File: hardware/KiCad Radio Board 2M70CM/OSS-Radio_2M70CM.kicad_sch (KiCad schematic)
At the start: 110 parts, among them J1 DF40C-24DP-0.4V, Q1 BSS138, Q2 BSS138, Q3 BSS138, U3 GRF5504, U4 TPS7A4701xRGW, U5 CC1200, U6 AT24CS01-STUM, U7 SKY13330-397LF, Y4 TG-5021CG

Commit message: changed mounting holes on 2M70CM board
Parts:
- removed TP4: TestPoint, TestPoint:TestPoint_Pad_D1.0mm, symbol Connector:TestPoint
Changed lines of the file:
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@@
 	)
 	(junction
-		(at 243.84 26.67)
-		(diameter 0)
-		(color 0 0 0 0)
-	)
-	(junction
 		(at 121.92 158.75)
 		(diameter 0)
@@
 	(wire
 		(pts
-			(xy 228.6 26.67) (xy 243.84 26.67)
+			(xy 228.6 26.67) (xy 246.38 26.67)
 		)
 		(stroke
@@
 	(wire
 		(pts
-			(xy 243.84 26.67) (xy 246.38 26.67)
-		)
-		(stroke
-			(width 0)
-			(type default)
-		)
-	)
-	(wire
-		(pts
 			(xy 147.32 93.98) (xy 180.34 93.98)
 		)
@@
 					(unit 1)
 				)
-			)
-		)
-	)
-	(symbol
-		(lib_id "Connector:TestPoint")
-		(at 243.84 26.67 180)
-		(unit 1)
-		(exclude_from_sim no)
-		(in_bom no)
-		(on_board yes)
-		(dnp no)
-		(fields_autoplaced yes)
-		(property "Reference" "TP4"
-			(at 246.38 28.7019 0)
-			(effects
-				(font
-					(size 1.27 1.27)
-				)
-				(justify right)
-			)
-		)
-		(property "Value" "TestPoint"
-			(at 246.38 31.2419 0)
-			(effects
-				(font
-					(size 1.27 1.27)
-				)
-				(justify right)
-			)
-		)
-		(property "Footprint" "TestPoint:TestPoint_Pad_D1.0mm"
-			(at 238.76 26.67 0)
-			(effects
-				(font
-					(size 1.27 1.27)
-				)
-				(hide yes)
-			)
-		)
-		(property "Datasheet" "~"
-			(at 238.76 26.67 0)
-			(effects
-				(font
-					(size 1.27 1.27)
-				)
-				(hide yes)
-			)
-		)
-		(property "Description" "test point"
-			(at 243.84 26.67 0)
-			(effects
-				(font
-					(size 1.27 1.27)
-				)
-				(hide yes)
-			)
-		)
-		(pin "1"
-		)
-		(instances
-			(project "OSS-Radio_2M70CM"
-				(path "/07417920-d864-4fe6-bbe4-9feb9e01fbee"
-					(reference "TP4")
-					(unit 1)
-				)

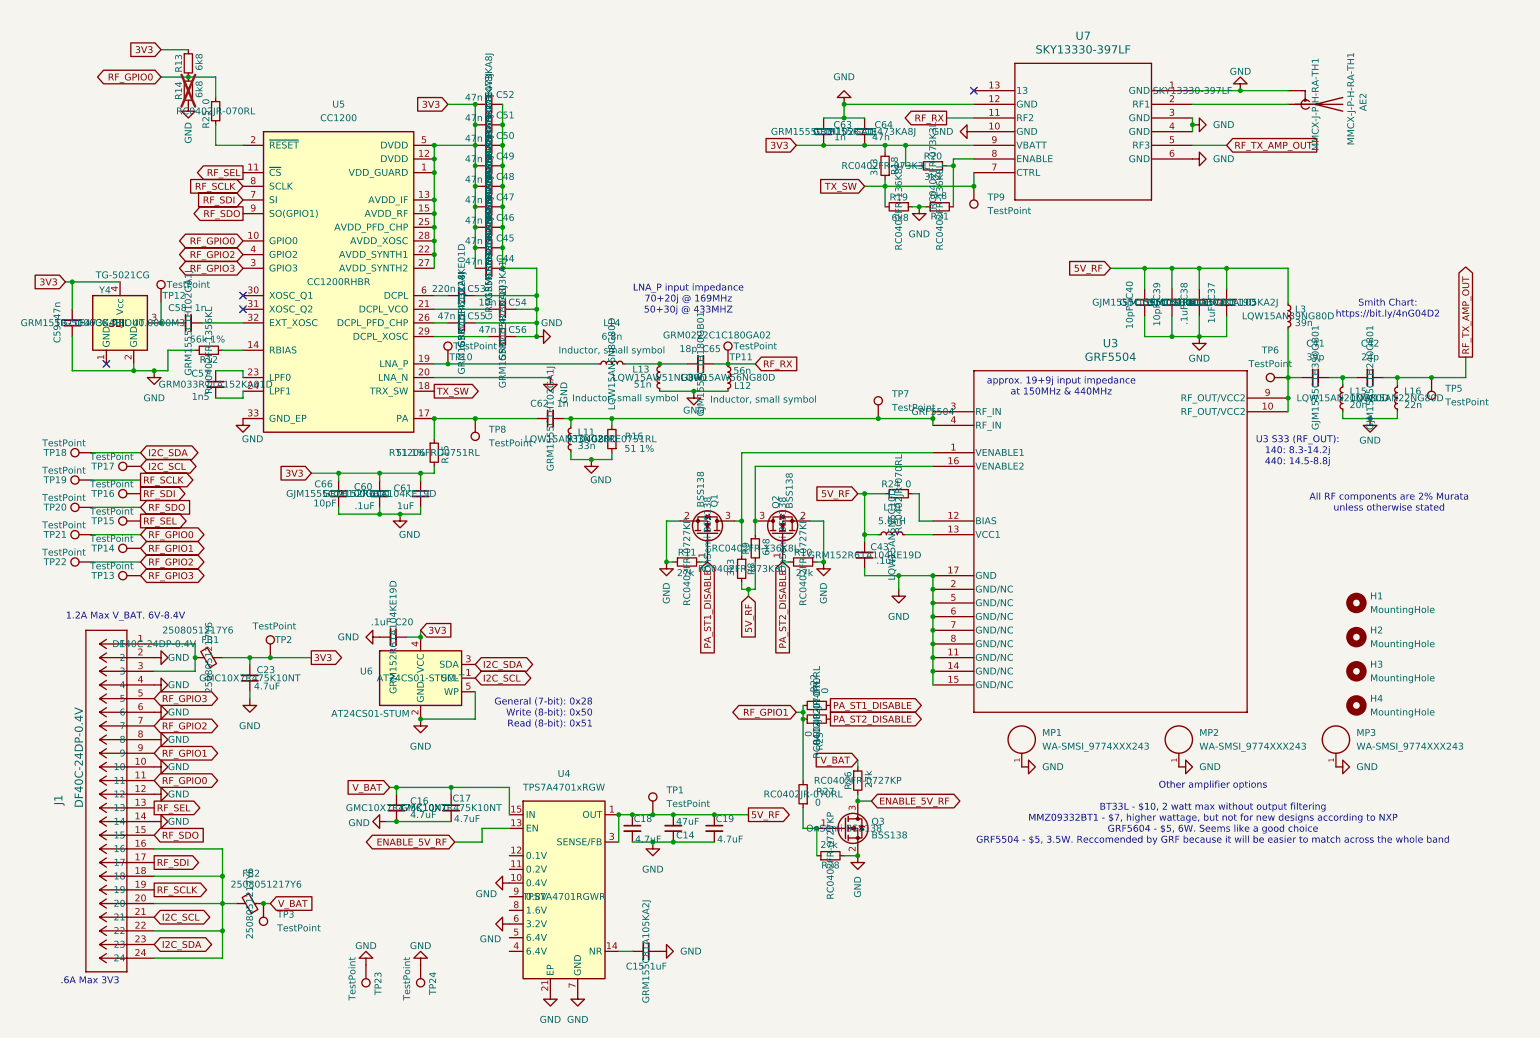
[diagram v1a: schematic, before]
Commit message: changed schematic annotations to not show part numbers
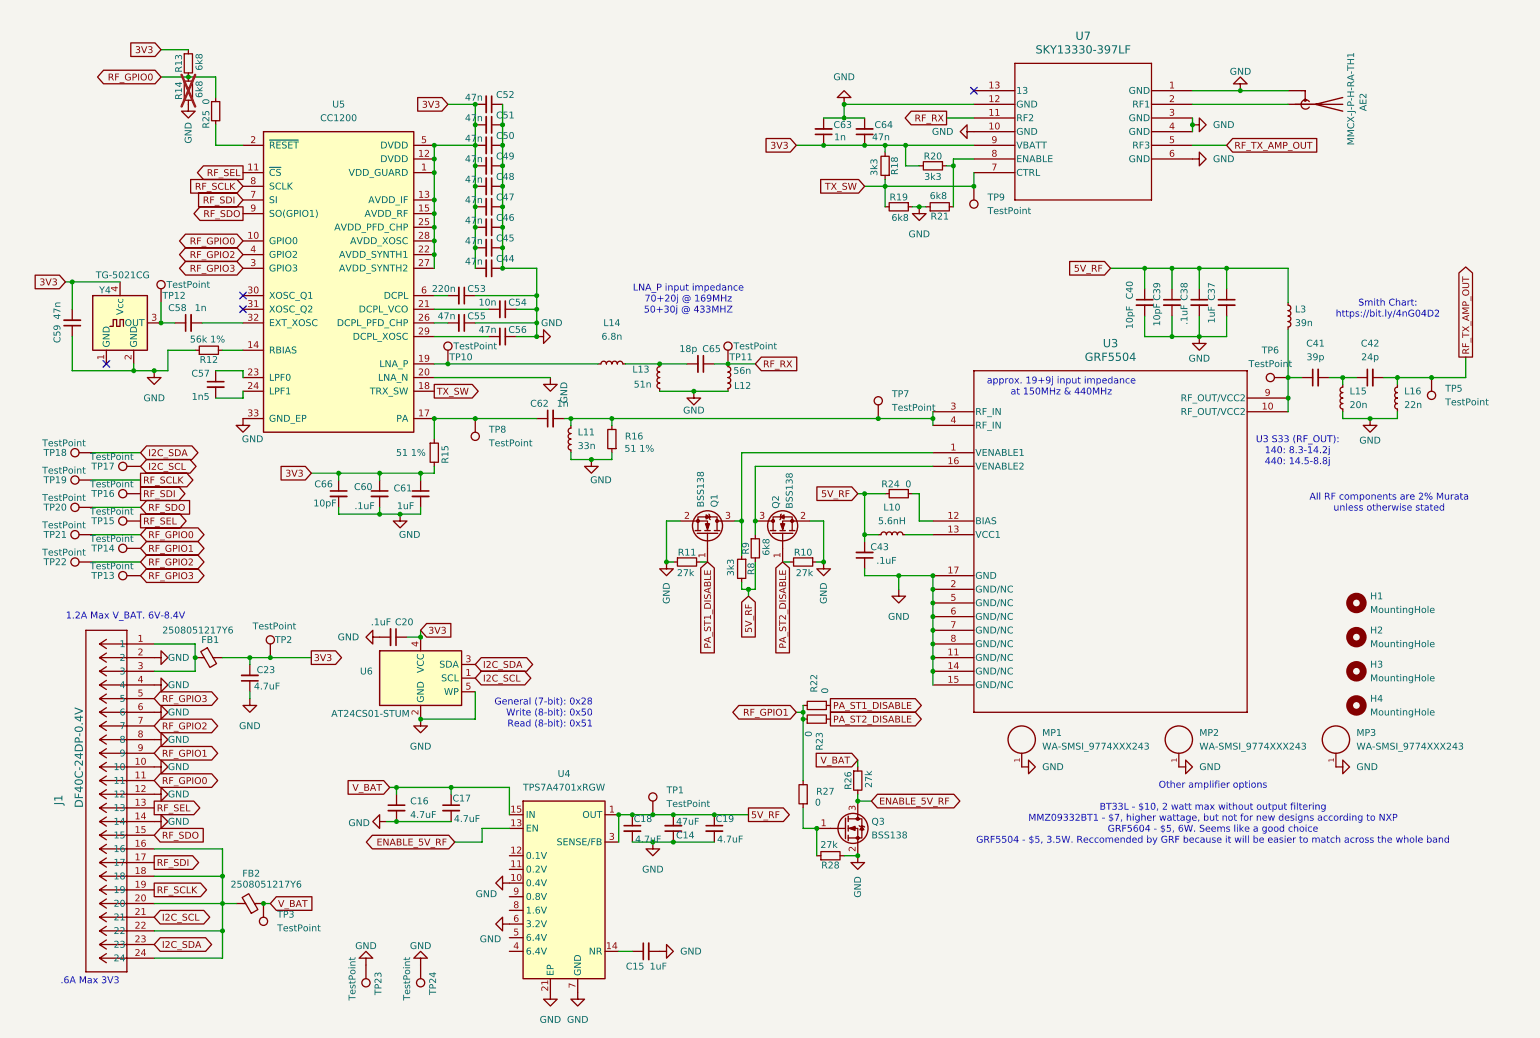
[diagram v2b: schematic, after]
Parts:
- AE2, C14, C15, C16, C17, C18, C19, C20, C23, C37, C38, C39, C40, C41, C42, C43, C44, C45, C46, C47, C48, C49, C50, C51, C52, C53, C54, C55, C56, C57, C58, C59, C60, C61, C62, C63, C64, C65, C66, FB1, FB2, J1, L10, L11, L12, L13, L14, L15, L16, L3, MP1, MP2, MP3, Q1, Q2, Q3, R10, R11, R12, R13, R15, R16, R18, R19, R20, R21, R22, R23, R24, R25, R26, R27, R28, R8, R9, U3, U4, U5, U6, U7, Y4: now left out of the parts list

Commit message: Rev 0.2, added 0 ohm resistor on GPIO0, fixed some DRC errors and added optional pogo pin power interface if needed
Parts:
- added J2, J3: P70-7000045, TestPoint:TestPoint_Pad_D1.5mm, symbol Connector:TestPoint
- added R29: 0, Resistor_SMD:R_0402_1005Metric, symbol Device:R_Small
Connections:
- net GND: now also J3.1
- net RF_GPIO0: now also R29.2; no longer U5.10 (GPIO0)
- net at FB2.2, J1.16, J1.18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: now also J2.1
- new net: R29.1, U5.10 (GPIO0)

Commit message: fixed pogo foorprints and did rev 0.2 exports
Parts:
- J2, J3: now not fitted
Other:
- moved on the sheet: C65
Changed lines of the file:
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@@
 	(wire
 		(pts
-			(xy 139.7 74.93) (xy 142.24 74.93)
+			(xy 138.43 74.93) (xy 142.24 74.93)
 		)
 		(stroke
@@
 	(wire
 		(pts
-			(xy 129.54 74.93) (xy 134.62 74.93)
+			(xy 129.54 74.93) (xy 133.35 74.93)
 		)
 		(stroke
@@
 		(in_bom yes)
 		(on_board yes)
-		(dnp no)
+		(dnp yes)
 		(property "Reference" "J3"
 			(at 57.912 191.77 90)
@@
 		(in_bom yes)
 		(on_board yes)
-		(dnp no)
+		(dnp yes)
 		(property "Reference" "J2"
 			(at 54.356 189.23 90)
@@
 	(symbol
 		(lib_id "Device:C_Small")
-		(at 137.16 74.93 270)
+		(at 135.89 74.93 270)
 		(unit 1)
 		(exclude_from_sim no)
@@
 		(dnp no)
 		(property "Reference" "C65"
-			(at 139.192 72.136 90)
+			(at 137.922 72.136 90)
 			(effects
 				(font
@@
 		)
 		(property "Value" "18p"
-			(at 134.874 72.136 90)
+			(at 133.604 72.136 90)
 			(effects
 				(font
@@
 		)
 		(property "Footprint" "Capacitor_SMD:C_0402_1005Metric"
-			(at 137.16 74.93 0)
+			(at 135.89 74.93 0)
 			(effects
 				(font
@@
 		)
 		(property "Datasheet" "~"
-			(at 137.16 74.93 0)
+			(at 135.89 74.93 0)
 			(effects
 				(font
@@
 		)
 		(property "Description" ""
-			(at 140.208 69.596 90)
+			(at 138.938 69.596 90)
 			(effects
 				(font
@@
 		)
 		(property "PART-NUMBER" "GJM1555C1H180GB01"
-			(at 137.16 74.93 0)
+			(at 135.89 74.93 0)
 			(effects
 				(font

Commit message: fixed BOM and CPL for JLCPCB
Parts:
- AE2, C14, C15, C16, C17, C18, C19, C20, C23, C37, C38, C39, C40, C41, C42, C43, C44, C45, C46, C47, C48, C49, C50, C51, C52, C53, C54, C55, C56, C57, C58, C59, C60, C61, C62, C63, C64, C65, C66, FB1, FB2, H1, H2, H3, H4, J1, L10, L11, L12, L13, L14, L15, L16, L3, MP1, MP2, MP3, Q1, Q2, Q3, R10, R11, R12, R13, R14, R15, R16, R18, R19, R20, R21, R22, R23, R24, R25, R26, R27, R28, R29, R8, R9, TP1, TP10, TP11, TP12, TP13, TP14, TP15, TP16, TP17, TP18, TP19, TP2, TP20, TP21, TP22, TP23, TP24, TP3, TP5, TP6, TP7, TP8, TP9, U3, U4, U5, U6, U7, Y4: now in the parts list

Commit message: added jlcpcb part numbers to BOM
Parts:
- AE2: JLCPB Part# (none) -> C2934607
- C14: JLCPB Part# (none) -> C7198516
- C15, C37, C61: JLCPB Part# (none) -> C3856634
- C16, C17, C18, C19, C23: JLCPB Part# (none) -> C6203961
- C20, C38, C43, C60: JLCPB Part# (none) -> C71629; PART-NUMBER GRM152R61A104KE19D -> GRM155R71C104KA88D
- C39, C40, C66: JLCPB Part# (none) -> C85873
- C41: JLCPB Part# (none) -> C1864241
- C42: JLCPB Part# (none) -> C1864641
- C44, C45, C46, C47, C48, C49, C50, C51, C52, C55, C56, C59, C64: JLCPB Part# (none) -> C2168499
- C53: JLCPB Part# (none) -> C5755009
- C54: JLCPB Part# (none) -> C85735; PART-NUMBER GRM155R71E103KA1J -> GRM155R71C103KA01D
- C57: JLCPB Part# (none) -> C710829
- C58, C62, C63: JLCPB Part# (none) -> C1852376
- C65: JLCPB Part# (none) -> C237274
- FB1, FB2: JLCPB Part# (none) -> C3716596
- H1, H2, H3, H4, TP1, TP10, TP11, TP12, TP13, TP14, TP15, TP16, TP17, TP18, TP19, TP2, TP20, TP21, TP22, TP23, TP24, TP3, TP5, TP6, TP7, TP8, TP9: now left out of the parts list
- J1: JLCPB Part# (none) -> C424639
- J2, J3: JLCPB Part# (none) -> C21344921; PART-NUMBER (none) -> P70-7000045
- L10: JLCPB Part# (none) -> C91626
- L11: JLCPB Part# (none) -> C2043859
- L12: JLCPB Part# (none) -> C1012790
- L13: JLCPB Part# (none) -> C1012789
- L14: JLCPB Part# (none) -> C882467
- L15: JLCPB Part# (none) -> C2043868
- L16: JLCPB Part# (none) -> C524641
- L3: JLCPB Part# (none) -> C269823
- MP1, MP2, MP3: JLCPB Part# (none) -> C19725753
- Q1, Q2, Q3: JLCPB Part# (none) -> C52895
- R10, R11, R26, R28: JLCPB Part# (none) -> C5716745
- R12: JLCPB Part# (none) -> C4193995
- R13, R14, R19, R21, R9: JLCPB Part# (none) -> C4016348
- R15: JLCPB Part# (none) -> C862185
- R16: JLCPB Part# (none) -> C854359
- R18, R20, R8: JLCPB Part# (none) -> C137992
- R22, R23, R24, R25, R27, R29: JLCPB Part# (none) -> C60485
- U3: JLCPB Part# (none) -> C5379863
- U4: JLCPB Part# (none) -> C90084
- U5: JLCPB Part# (none) -> C122881
- U6: JLCPB Part# (none) -> C616257
- U7: JLCPB Part# (none) -> C2654715
- Y4: JLCPB Part# (none) -> C5797117

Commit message: changed some components on BOM in order to get them easier from JLC
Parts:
- C14: JLCPB Part# C7198516 -> C77101; PART-NUMBER GRJ32ER71A476KE11L -> GRM32ER61C476KE15L
- C15, C37, C61: JLCPB Part# C3856634 -> C77006; PART-NUMBER GRM155C81A105KA2J -> GRM155R61C105KA12D
- C16, C17, C18, C19, C23: JLCPB Part# C6203961 -> C77045; PART-NUMBER GMC10X7R475K10NT -> GRM188R61C475KE11D
- C44, C45, C46, C47, C48, C49, C50, C51, C52, C55, C56, C59, C64: JLCPB Part# C2168499 -> C77017; PART-NUMBER GRM155R71E473KA8J -> GRM155R71E473KA88D
- C53: JLCPB Part# C5755009 -> C77011; PART-NUMBER GRM15R61J224KE01D -> GRM155R71C224KA12D
- C57: JLCPB Part# C710829 -> C161482; PART-NUMBER GRM033R71A152KA01D -> GRM033R71C152KA01D
- FB1, FB2: value 2508051217Y6 -> BLM21PG121SN1D; JLCPB Part# C3716596 -> C79382; PART-NUMBER 2508051217Y6 -> BLM21PG121SN1D
- L12: now not fitted
- MP1, MP2, MP3: JLCPB Part# C19725753 -> C22431324; PART-NUMBER 9774015943R -> 9774015243R
- R13, R14, R19, R21, R9: JLCPB Part# C4016348 -> C965237; PART-NUMBER RC0402FR-136K8L -> NQ02WGF6801TCE

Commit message: updated BOM for new RF oscillator
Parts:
- Y4: JLCPB Part# C5797117 -> C20341501; PART-NUMBER TG-5006CG-43L 40.0000M3 -> TG2520SMN 40.0000M-CCGNDM5
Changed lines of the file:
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@@
 			)
 		)
-		(property "PART-NUMBER" "TG-5006CG-43L 40.0000M3"
+		(property "PART-NUMBER" "TG2520SMN 40.0000M-CCGNDM5"
 			(at 29.21 67.31 0)
 			(effects
@@
 			)
 		)
-		(property "JLCPB Part#" "C5797117"
+		(property "JLCPB Part#" "C20341501"
 			(at 29.21 67.31 0)
 			(effects
